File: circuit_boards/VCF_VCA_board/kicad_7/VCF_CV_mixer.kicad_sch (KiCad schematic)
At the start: 23 parts, among them U6 TL072

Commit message: Progress on circuit boards
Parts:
- SW? (x4): value E-Switch_EG2201 -> E-Switch_EG2201B
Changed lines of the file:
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@@
   (title_block
     (title "MICRO-OX VCF/VCA board")
-    (date "2023-03-21")
+    (date "2023-04-13")
     (rev "0")
     (comment 1 "creativecommons.org/licenses/by/4.0/")
@@
       (effects (font (size 1.27 1.27)))
     )
-    (property "Value" "E-Switch_EG2201" (at 204.47 148.59 0)
+    (property "Value" "E-Switch_EG2201B" (at 204.47 148.59 0)
       (effects (font (size 1.27 1.27)))
     )
@@
   (symbol (lib_id "custom_symbols:E-Switch_EG2201") (at 133.35 157.48 0) (mirror y) (unit 1)
     (in_bom yes) (on_board yes) (dnp no) (fields_autoplaced)
-    (property "Reference" "SW?" (at 133.35 149.86 0)
-      (effects (font (size 1.27 1.27)))
-    )
-    (property "Value" "E-Switch_EG2201" (at 133.35 152.4 0)
+    (property "Reference" "SW?" (at 133.35 151.13 0)
+      (effects (font (size 1.27 1.27)))
+    )
+    (property "Value" "E-Switch_EG2201B" (at 133.35 153.67 0)
       (effects (font (size 1.27 1.27)))
     )
@@
   (symbol (lib_id "custom_symbols:E-Switch_EG2201") (at 133.35 85.09 0) (mirror y) (unit 1)
     (in_bom yes) (on_board yes) (dnp no) (fields_autoplaced)
-    (property "Reference" "SW?" (at 133.35 77.47 0)
-      (effects (font (size 1.27 1.27)))
-    )
-    (property "Value" "E-Switch_EG2201" (at 133.35 80.01 0)
+    (property "Reference" "SW?" (at 133.35 78.74 0)
+      (effects (font (size 1.27 1.27)))
+    )
+    (property "Value" "E-Switch_EG2201B" (at 133.35 81.28 0)
       (effects (font (size 1.27 1.27)))
     )
@@
       (effects (font (size 1.27 1.27)))
     )
-    (property "Value" "E-Switch_EG2201" (at 269.24 148.59 0)
-      (effects (font (size 1.27 1.27)))
-    )
+    (property "Value" "E-Switch_EG2201B" (at 269.24 148.59 0)
+      (effects (font (size 1.27 1.27)))
+    )

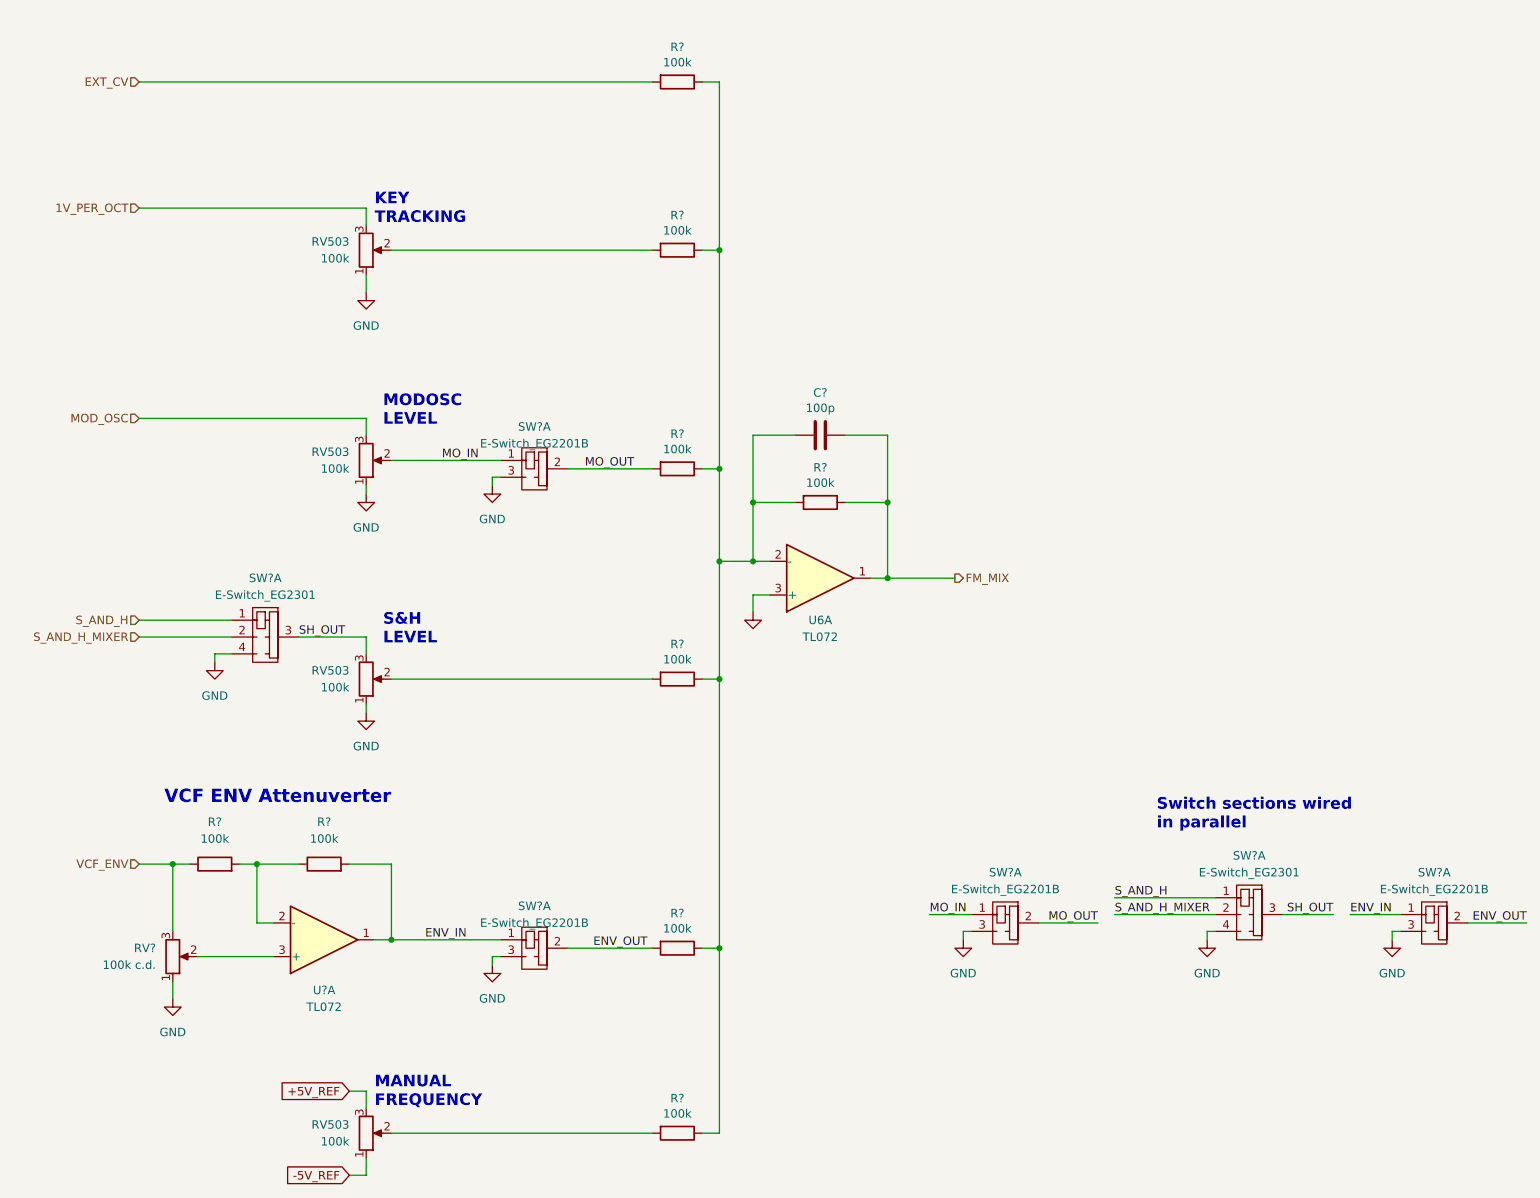
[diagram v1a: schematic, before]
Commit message: Update PCBs, tweak vals, add VCF CV from DAC
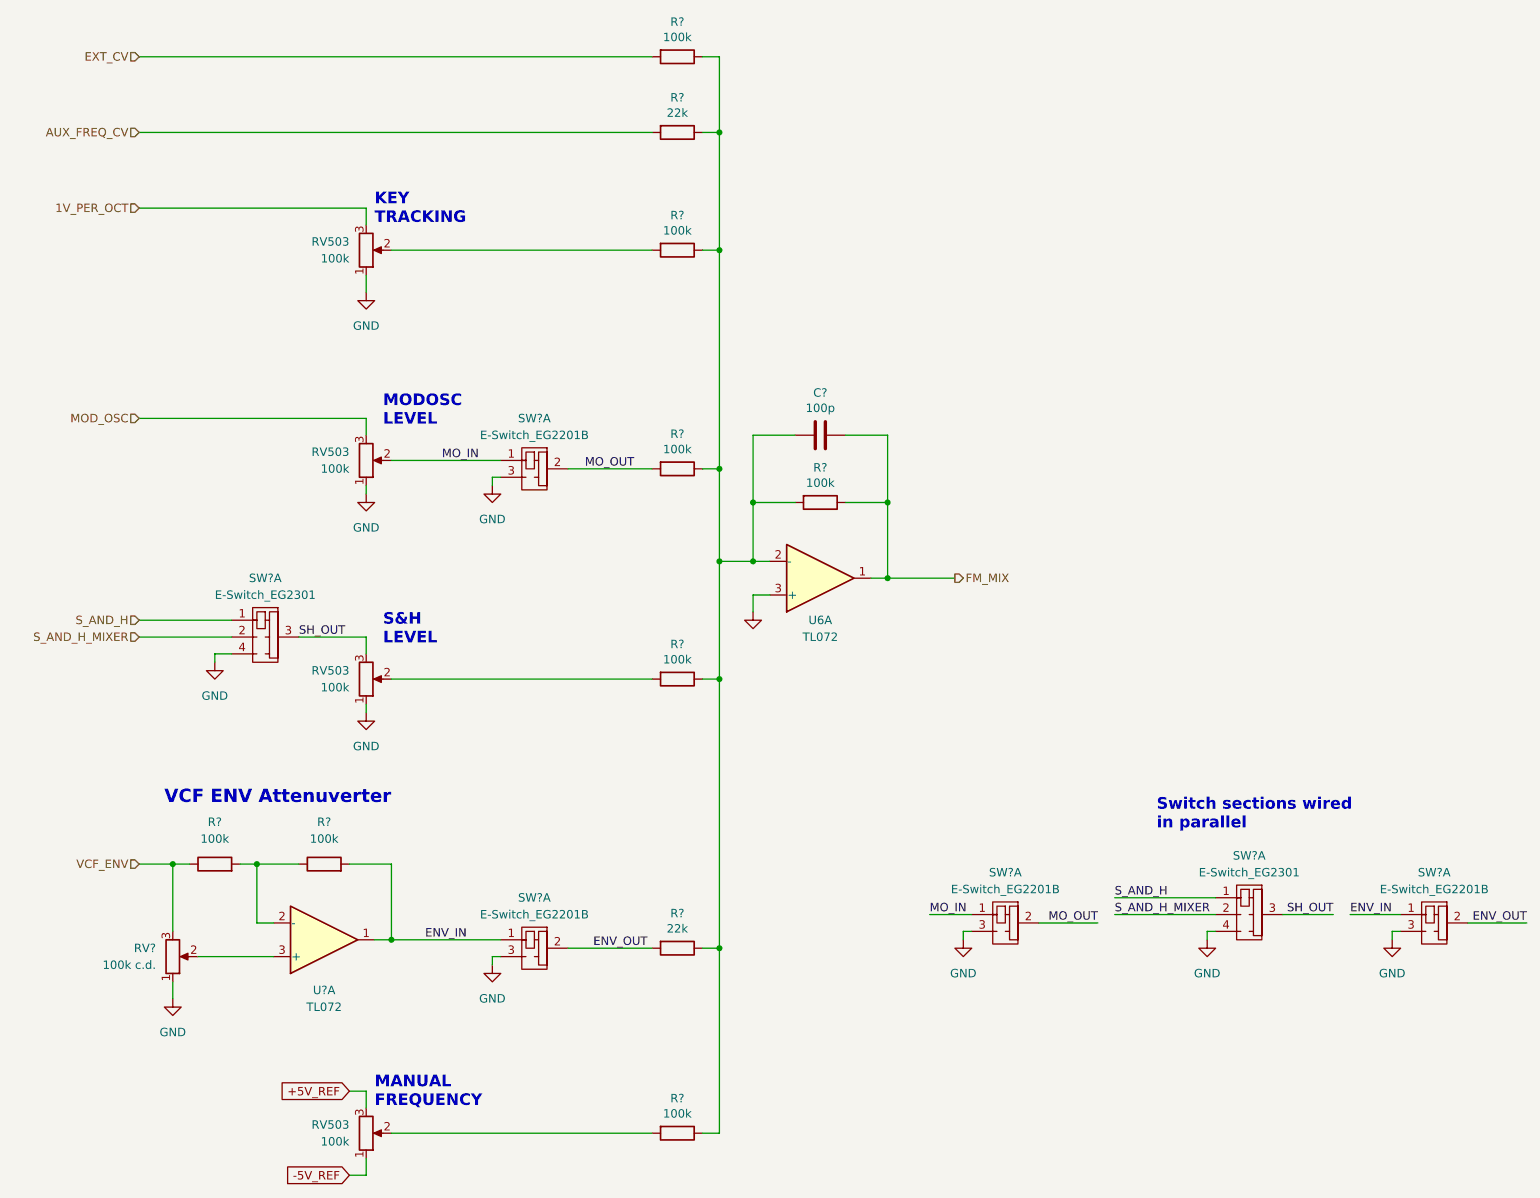
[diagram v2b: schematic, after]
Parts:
- added R?: 22k, Resistor_SMD:R_0603_1608Metric, symbol Device:R
- R?: value 100k -> 22k
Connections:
- net at C?.2, R?.1, R?.1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: now also R?.1
- new net AUX_FREQ_CV: R?.2
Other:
- moved on the sheet: R?
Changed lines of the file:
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@@
   (title_block
     (title "MICRO-OX VCF/VCA board")
-    (date "2023-04-13")
-    (rev "0")
+    (date "2023-04-25")
+    (rev "0.1")
     (comment 1 "creativecommons.org/licenses/by/4.0/")
     (comment 2 "License: CC by 4.0")
@@
   (junction (at 161.29 52.07) (diameter 0) (color 0 0 0 0)
   )
+  (junction (at 161.29 34.29) (diameter 0) (color 0 0 0 0)
+  )
   (junction (at 161.29 116.84) (diameter 0) (color 0 0 0 0)
   )
@@
     (stroke (width 0) (type default))
   )
+  (wire (pts (xy 161.29 34.29) (xy 161.29 52.07))
+    (stroke (width 0) (type default))
+  )
   (wire (pts (xy 166.37 99.06) (xy 161.29 99.06))
     (stroke (width 0) (type default))
   )
-  (wire (pts (xy 161.29 26.67) (xy 161.29 52.07))
+  (wire (pts (xy 161.29 22.86) (xy 161.29 34.29))
     (stroke (width 0) (type default))
   )
@@
     (stroke (width 0) (type default))
   )
-  (wire (pts (xy 158.75 26.67) (xy 161.29 26.67))
+  (wire (pts (xy 158.75 22.86) (xy 161.29 22.86))
     (stroke (width 0) (type default))
   )
@@
     (stroke (width 0) (type default))
   )
+  (wire (pts (xy 73.66 34.29) (xy 151.13 34.29))
+    (stroke (width 0) (type default))
+  )
   (wire (pts (xy 262.89 156.21) (xy 262.89 154.94))
     (stroke (width 0) (type default))
@@
     (stroke (width 0) (type default))
   )
-  (wire (pts (xy 73.66 26.67) (xy 151.13 26.67))
+  (wire (pts (xy 73.66 22.86) (xy 151.13 22.86))
+    (stroke (width 0) (type default))
+  )
+  (wire (pts (xy 158.75 34.29) (xy 161.29 34.29))
     (stroke (width 0) (type default))
   )
@@
     (effects (font (size 1.27 1.27)) (justify right))
   )
-  (hierarchical_label "EXT_CV" (shape input) (at 73.66 26.67 180) (fields_autoplaced)
+  (hierarchical_label "EXT_CV" (shape input) (at 73.66 22.86 180) (fields_autoplaced)
+    (effects (font (size 1.27 1.27)) (justify right))
+  )
+  (hierarchical_label "AUX_FREQ_CV" (shape input) (at 73.66 34.29 180) (fields_autoplaced)
     (effects (font (size 1.27 1.27)) (justify right))
   )
@@
   )
   (symbol (lib_id "custom_symbols:E-Switch_EG2201") (at 133.35 157.48 0) (mirror y) (unit 1)
-    (in_bom yes) (on_board yes) (dnp no) (fields_autoplaced)
-    (property "Reference" "SW?" (at 133.35 151.13 0)
-      (effects (font (size 1.27 1.27)))
-    )
-    (property "Value" "E-Switch_EG2201B" (at 133.35 153.67 0)
+    (in_bom yes) (on_board yes) (dnp no)
+    (property "Reference" "SW?" (at 133.35 149.86 0)
+      (effects (font (size 1.27 1.27)))
+    )
+    (property "Value" "E-Switch_EG2201B" (at 133.35 152.4 0)
       (effects (font (size 1.27 1.27)))
     )
@@
     )
   )
+  (symbol (lib_id "Device:R") (at 154.94 34.29 270) (unit 1)
+    (in_bom yes) (on_board yes) (dnp no)
+    (property "Reference" "R?" (at 154.94 29.0322 90)
+      (effects (font (size 1.27 1.27)))
+    )
+    (property "Value" "22k" (at 154.94 31.3436 90)
+      (effects (font (size 1.27 1.27)))
+    )
+    (property "Footprint" "Resistor_SMD:R_0603_1608Metric" (at 154.94 32.512 90)
+      (effects (font (size 1.27 1.27)) hide)
+    )
+    (property "Datasheet" "~" (at 154.94 34.29 0)
+      (effects (font (size 1.27 1.27)) hide)
+    )
+    (pin "1")
+    (pin "2")
+    (instances
+      (project "main_VCO_board"
+        (path "/2ebbd822-cb2c-491c-a836-3897c27c2326/40c396b5-96c3-4ce6-8ea1-40db52395d78"
+          (reference "R?") (unit 1)
+        )
+        (path "/2ebbd822-cb2c-491c-a836-3897c27c2326/9d6c03c4-3aa0-4313-a0ad-de5a4f8fba64"
+          (reference "R?") (unit 1)
+        )
+      )
+      (project "VCF_VCA_board"
+        (path "/aeb6db35-7681-4421-a39a-082f6f25fdc3/750d5855-94aa-4245-8612-ee86db261f77"
+          (reference "R410") (unit 1)
+        )
+      )
+    )
+  )
   (symbol (lib_id "power:GND") (at 166.37 106.68 0) (unit 1)
     (in_bom yes) (on_board yes) (dnp no)
@@
     )
   )
-  (symbol (lib_id "Device:R") (at 154.94 26.67 270) (unit 1)
+  (symbol (lib_id "Device:R") (at 154.94 22.86 270) (unit 1)
     (in_bom yes) (on_board yes) (dnp no)
-    (property "Reference" "R?" (at 154.94 21.4122 90)
-      (effects (font (size 1.27 1.27)))
-    )
-    (property "Value" "100k" (at 154.94 23.7236 90)
-      (effects (font (size 1.27 1.27)))
-    )
-    (property "Footprint" "Resistor_SMD:R_0603_1608Metric" (at 154.94 24.892 90)
-      (effects (font (size 1.27 1.27)) hide)
-    )
-    (property "Datasheet" "~" (at 154.94 26.67 0)
+    (property "Reference" "R?" (at 154.94 17.6022 90)
+      (effects (font (size 1.27 1.27)))
+    )
+    (property "Value" "100k" (at 154.94 19.9136 90)
+      (effects (font (size 1.27 1.27)))
+    )
+    (property "Footprint" "Resistor_SMD:R_0603_1608Metric" (at 154.94 21.082 90)
+      (effects (font (size 1.27 1.27)) hide)
+    )
+    (property "Datasheet" "~" (at 154.94 22.86 0)
       (effects (font (size 1.27 1.27)) hide)
     )
@@
   )
   (symbol (lib_id "custom_symbols:E-Switch_EG2201") (at 133.35 85.09 0) (mirror y) (unit 1)
-    (in_bom yes) (on_board yes) (dnp no) (fields_autoplaced)
-    (property "Reference" "SW?" (at 133.35 78.74 0)
-      (effects (font (size 1.27 1.27)))
-    )
-    (property "Value" "E-Switch_EG2201B" (at 133.35 81.28 0)
+    (in_bom yes) (on_board yes) (dnp no)
+    (property "Reference" "SW?" (at 133.35 77.47 0)
+      (effects (font (size 1.27 1.27)))
+    )
+    (property "Value" "E-Switch_EG2201B" (at 133.35 80.01 0)
       (effects (font (size 1.27 1.27)))
     )
@@
       (effects (font (size 1.27 1.27)))
     )
-    (property "Value" "100k" (at 154.94 154.5336 90)
-      (effects (font (size 1.27 1.27)))
-    )
+    (property "Value" "22k" (at 154.94 154.5336 90)
+      (effects (font (size 1.27 1.27)))
+    )

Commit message: Fix copy paste error with SSI2140 symbol, add potentiometer 3d model
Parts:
- RV503, RV?: footprint Potentiometer_THT:Potentiometer_Alpha_RD901F-40-00D_Single_Vertical -> custom_footprints:Potentiometer_Alpha_RD901F-40-00D_Single_Vertical
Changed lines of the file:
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@@
       (effects (font (size 1.27 1.27)) (justify right))
     )
-    (property "Footprint" "Potentiometer_THT:Potentiometer_Alpha_RD901F-40-00D_Single_Vertical" (at 107.95 116.84 0)
+    (property "Footprint" "custom_footprints:Potentiometer_Alpha_RD901F-40-00D_Single_Vertical" (at 107.95 116.84 0)
       (effects (font (size 1.27 1.27)) hide)
     )
@@
       (effects (font (size 1.27 1.27)) (justify right))
     )
-    (property "Footprint" "Potentiometer_THT:Potentiometer_Alpha_RD901F-40-00D_Single_Vertical" (at 78.74 158.75 0)
+    (property "Footprint" "custom_footprints:Potentiometer_Alpha_RD901F-40-00D_Single_Vertical" (at 78.74 158.75 0)
       (effects (font (size 1.27 1.27)) hide)
     )
@@
       (effects (font (size 1.27 1.27)) (justify right))
     )
-    (property "Footprint" "Potentiometer_THT:Potentiometer_Alpha_RD901F-40-00D_Single_Vertical" (at 107.95 83.82 0)
+    (property "Footprint" "custom_footprints:Potentiometer_Alpha_RD901F-40-00D_Single_Vertical" (at 107.95 83.82 0)
       (effects (font (size 1.27 1.27)) hide)
     )
@@
       (effects (font (size 1.27 1.27)) (justify right))
     )
-    (property "Footprint" "Potentiometer_THT:Potentiometer_Alpha_RD901F-40-00D_Single_Vertical" (at 107.95 52.07 0)
+    (property "Footprint" "custom_footprints:Potentiometer_Alpha_RD901F-40-00D_Single_Vertical" (at 107.95 52.07 0)
       (effects (font (size 1.27 1.27)) hide)
     )
@@
       (effects (font (size 1.27 1.27)) (justify right))
     )
-    (property "Footprint" "Potentiometer_THT:Potentiometer_Alpha_RD901F-40-00D_Single_Vertical" (at 107.95 185.42 0)
-      (effects (font (size 1.27 1.27)) hide)
-    )
+    (property "Footprint" "custom_footprints:Potentiometer_Alpha_RD901F-40-00D_Single_Vertical" (at 107.95 185.42 0)
+      (effects (font (size 1.27 1.27)) hide)
+    )
